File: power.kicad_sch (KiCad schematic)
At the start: 49 parts, among them IC3 CH224K, J5 USB_C_Receptacle_USB2.0, J6 Barrel_Jack, Q1 UTM6016G-SO8-R, Q13 CSD19537Q3, Q14 BSS138, U12 ETA7014, U13 TPD2EUSB30, U14 LM74700, U20 TPS5430DDA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

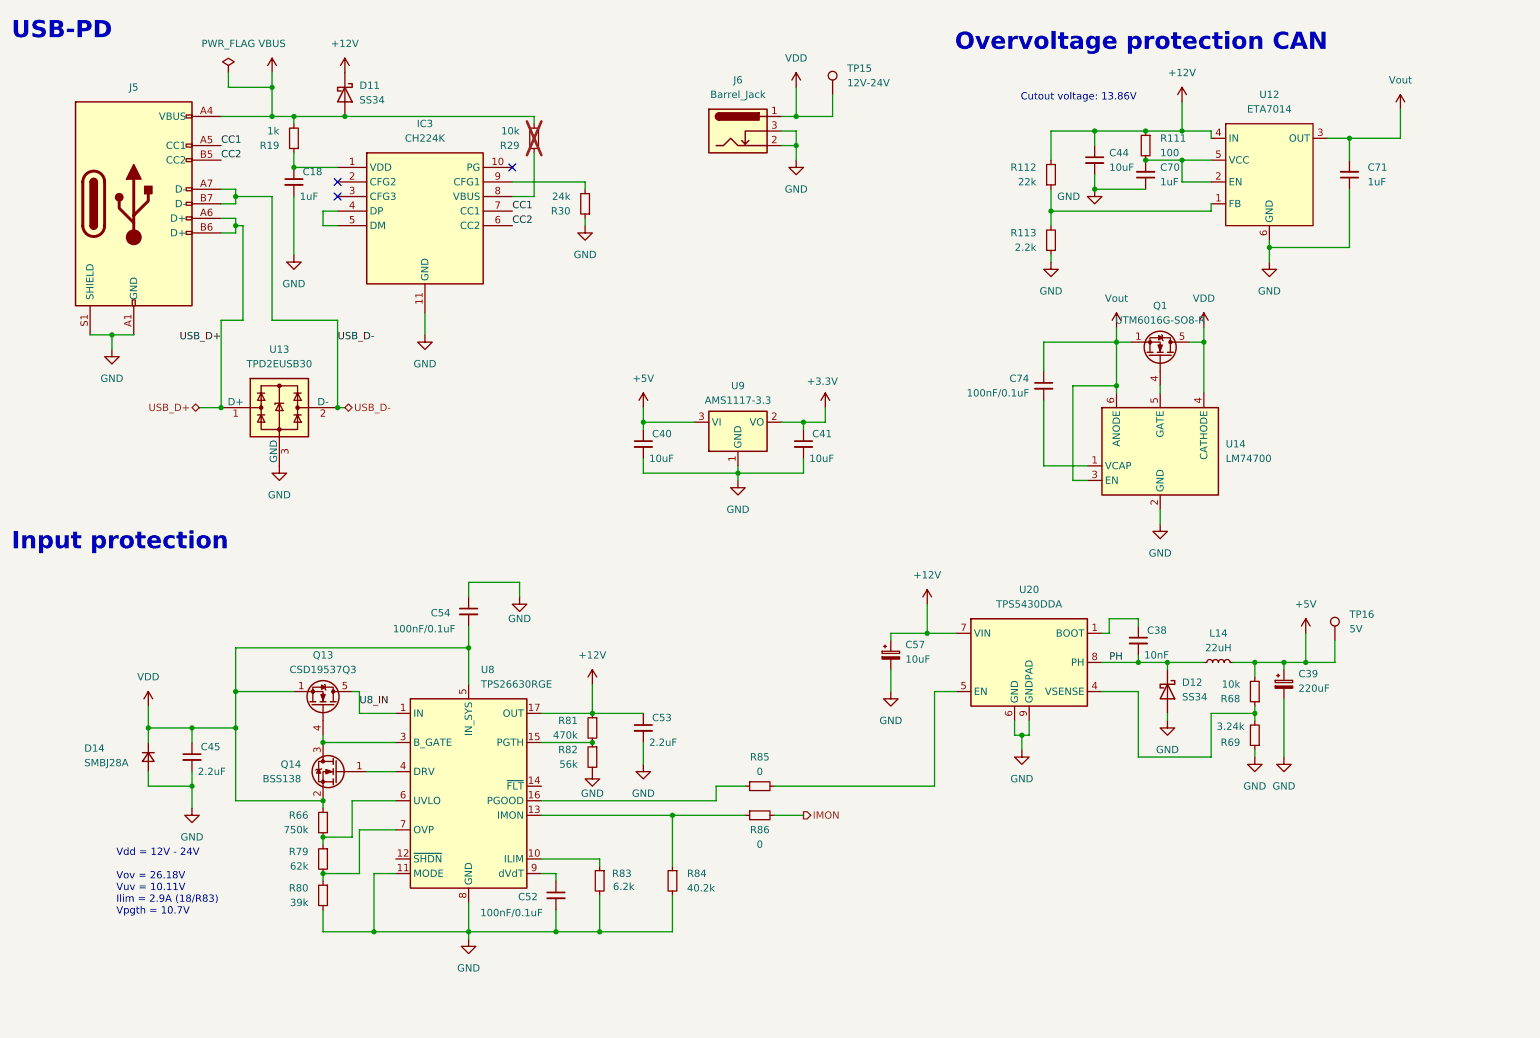
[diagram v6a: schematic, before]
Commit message: Replace diode for USB power with ideal diode
Closes #63
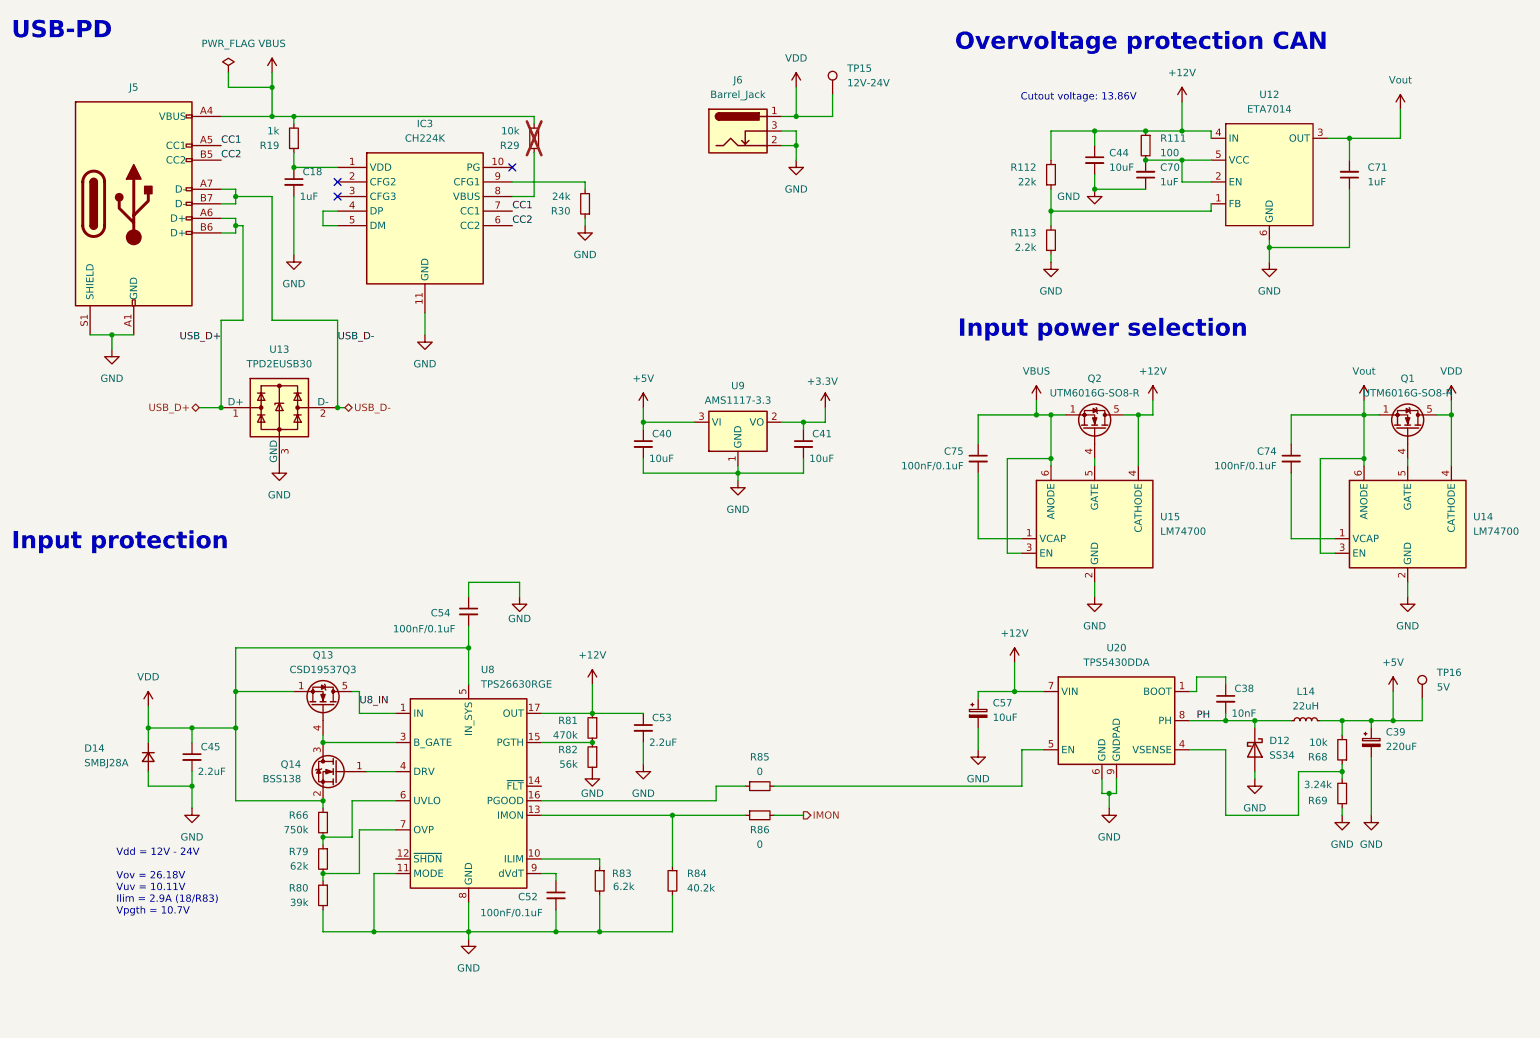
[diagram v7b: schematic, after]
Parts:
- removed D11: SS34, Diode_SMD:D_SMA, symbol Diode:SS34
- added C75: 100nF/0.1uF, Capacitor_SMD:C_0603_1608Metric, symbol Device:C_Small
- added Q2: UTM6016G-SO8-R, Package_SO:SOIC-8_3.9x4.9mm_P1.27mm, symbol Transistor_FET:IRF7403
- added U15: LM74700, Package_TO_SOT_SMD:SOT-23-6, symbol Power_Management:LM74700
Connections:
- net +12V: now also Q2.5 (D), Q2.6 (D), Q2.7 (D), Q2.8 (D), U15.4 (CATHODE)
- net GND: now also U15.2 (GND)
- net VBUS: now also C75.1, Q2.1 (S), Q2.2 (S), Q2.3 (S), U15.3 (EN), U15.6 (ANODE)
- new net: C75.2, U15.1 (VCAP)
- new net: Q2.4 (G), U15.5 (GATE)
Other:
- note added: "Input power selection"
- moved on the sheet: C38, C39, C57, C74, D12, L14, Q1, R68, R69, TP16, U14, U20

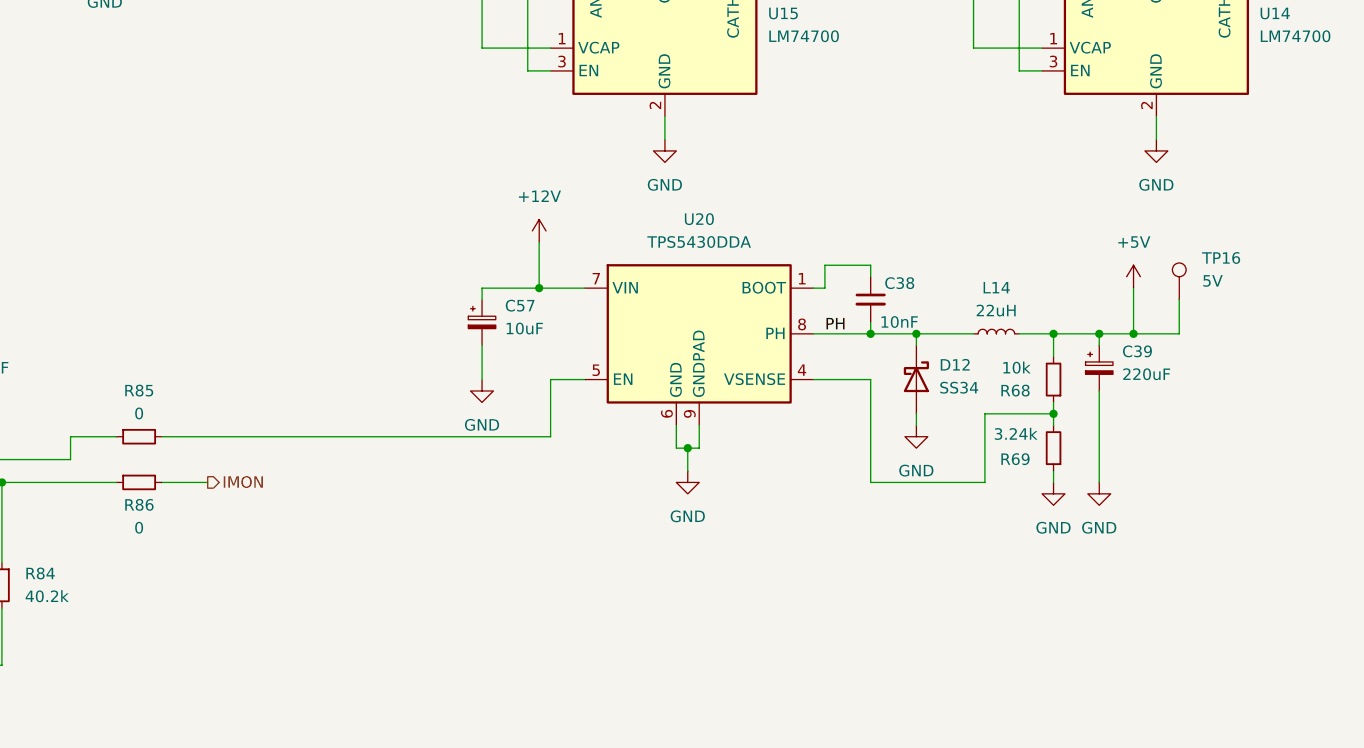
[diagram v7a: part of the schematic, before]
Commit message: Replace 5V stepdown with TPS62933
Closes #64
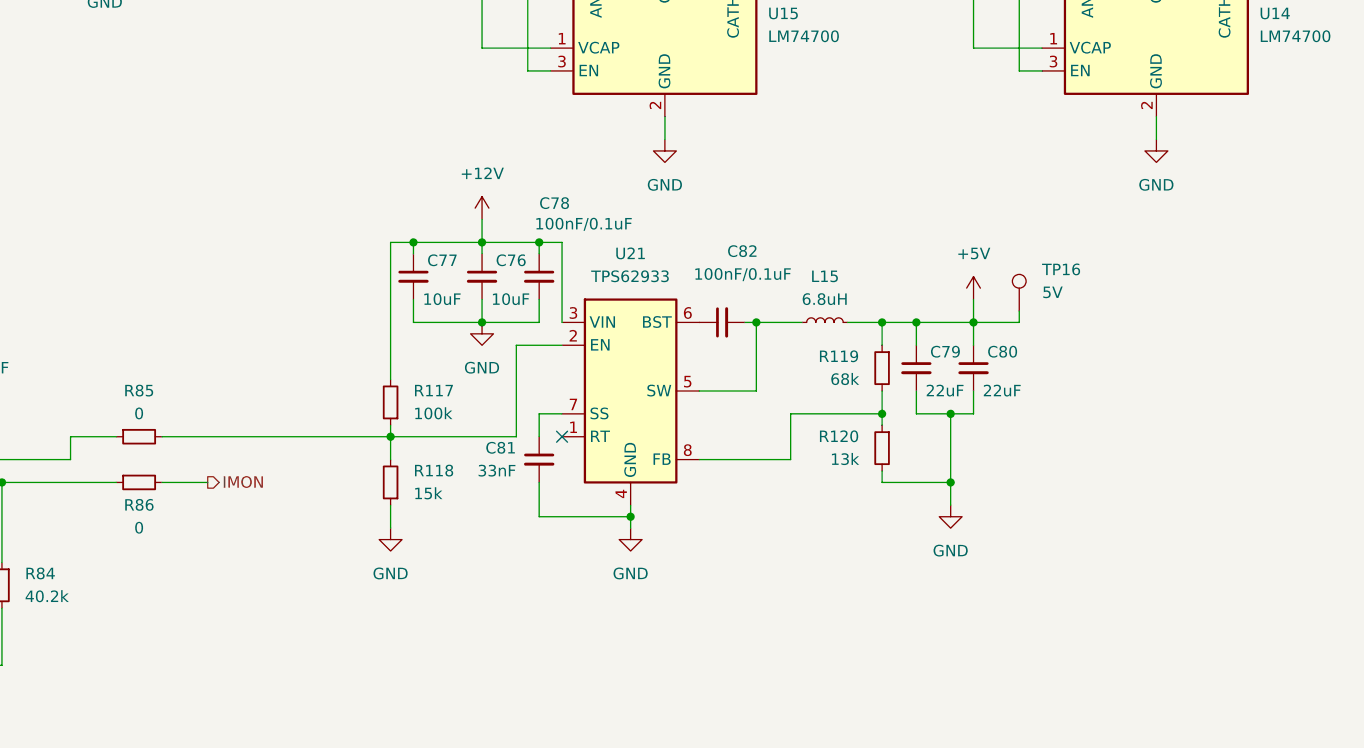
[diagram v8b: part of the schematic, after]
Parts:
- removed C38: 10nF, Capacitor_SMD:C_0603_1608Metric, symbol Device:C_Small
- removed C39: 220uF, Capacitor_SMD:CP_Elec_6.3x7.7, symbol Device:C_Polarized_Small
- removed C57: 10uF, Capacitor_SMD:CP_Elec_5x5.4, symbol Device:C_Polarized_Small
- removed D12: SS34, Diode_SMD:D_SMA, symbol Diode:SS34
- removed L14: 22uH, Inductor_SMD:L_Sunlord_SWPA8040S, symbol Device:L_Small
- removed R68: 10k, Resistor_SMD:R_0603_1608Metric, symbol Device:R_Small
- removed R69: 3.24k, Resistor_SMD:R_0603_1608Metric, symbol Device:R_Small
- removed U20: TPS5430DDA, Package_SO:TI_SO-PowerPAD-8_ThermalVias, symbol Regulator_Switching:TPS5430DDA
- added C76, C77: 10uF, Capacitor_SMD:C_1206_3216Metric, symbol Device:C_Small
- added C78, C82: 100nF/0.1uF, Capacitor_SMD:C_0402_1005Metric, symbol Device:C_Small
- added C79, C80: 22uF, Capacitor_SMD:C_1206_3216Metric, symbol Device:C_Small
- added C81: 33nF, Capacitor_SMD:C_0603_1608Metric, symbol Device:C_Small
- added L15: 6.8uH, Inductor_SMD:L_Sunlord_SWPA5040S, symbol Device:L_Small
- added R117: 100k, Resistor_SMD:R_0603_1608Metric, symbol Device:R_Small
- added R118: 15k, Resistor_SMD:R_0603_1608Metric, symbol Device:R_Small
- added R119: 68k, Resistor_SMD:R_0603_1608Metric, symbol Device:R_Small
- added R120: 13k, Resistor_SMD:R_0603_1608Metric, symbol Device:R_Small
- added U21: TPS62933, Package_TO_SOT_SMD:SOT-583-8, symbol Regulator_Switching:TPS62933
- C54: LCSC C1525 -> C307331
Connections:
- net +12V: now also C76.1, C77.1, C78.1, R117.2, U21.3 (VIN)
- net +5V: now also C79.1, C80.1, L15.2, R119.1
- net GND: now also C76.2, C77.2, C78.2, C79.2, C80.2, C81.2, R118.1, R120.2, U21.4 (GND)
- net at R85.2: now also R117.1, R118.2, U21.2 (EN)
- new net: C81.1, U21.7 (SS)
- new net: C82.1, U21.6 (BST)
- new net: C82.2, L15.1, U21.5 (SW)
- new net: R119.2, R120.1, U21.8 (FB)
- no-connect marks 3 -> 4
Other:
- moved on the sheet: TP16
